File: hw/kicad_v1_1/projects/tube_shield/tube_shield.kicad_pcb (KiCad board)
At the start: 2 copper layers, 100 x 75 mm, 25 parts, among them P1 CONN_02X12_isolate_hv, P2 CONN_01X01, P3 CONN_01X01, P4 CONN_01X01, P5 CONN_01X01, Q10 MPSA42, Q11 MPSA42, U1 K155ID1, U2 K155ID1, U3 K155ID1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

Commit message: Update
Begin work on updating for rev1.1.
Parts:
- removed Q10, Q11: MPSA42, TO_SOT_Packages_SMD:SOT-23_Handsoldering
- added Q1: MMBTA42, TO_SOT_Packages_SMD:SOT-23_Handsoldering, B.Cu at (126.2, 81.5)
- added Q2: MMBTA42, TO_SOT_Packages_SMD:SOT-23_Handsoldering, B.Cu at (131.2, 81.5)
- R30, R31, R32, R33: moved to B.Cu
- moved R30 27.2 mm to (126.5, 51.2), turned to 90 degrees
- moved R31 24.2 mm to (123.5, 51.2), turned to 90 degrees
- moved R2 17.0 mm to (102.2, 51.2)
- moved R33 13.7 mm to (131.5, 88.0), turned to 270 degrees
- moved R32 12.7 mm to (126.2, 88.0), turned to 270 degrees
- moved R1 12.6 mm to (136.5, 51.2), turned to 270 degrees
- moved P2 10.0 mm to (82.0, 51.0)
- moved P3 10.0 mm to (174.0, 51.0)
- moved N1 3.00 mm to (128.0, 65.2), turned to 270 degrees
- moved N2 3.00 mm to (128.0, 71.2), turned to 270 degrees
- moved R3 1.50 mm to (157.0, 51.2)
- moved R10 0.25 mm to (97.2, 51.2)
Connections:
- P1 pad 10: /Nixie Control/N1_SEL_C -> /Nixie Control/N2_SEL_C
- P1 pad 11: /Nixie Control/N0_SEL_D -> /Nixie Control/N3_SEL_D
- P1 pad 12: /Nixie Control/N1_SEL_D -> /Nixie Control/N2_SEL_D
- P1 pad 13: /Nixie Control/N2_SEL_A -> /Nixie Control/N0_SEL_A
- P1 pad 14: /Nixie Control/N3_SEL_A -> /Nixie Control/N1_SEL_A
- P1 pad 15: /Nixie Control/N2_SEL_B -> /Nixie Control/N0_SEL_B
- P1 pad 16: /Nixie Control/N3_SEL_B -> /Nixie Control/N1_SEL_B
- P1 pad 17: /Nixie Control/N2_SEL_C -> /Nixie Control/N0_SEL_C
- P1 pad 18: /Nixie Control/N3_SEL_C -> /Nixie Control/N1_SEL_C
- P1 pad 19: /Nixie Control/N2_SEL_D -> /Nixie Control/N0_SEL_D
- P1 pad 20: /Nixie Control/N3_SEL_D -> /Nixie Control/N1_SEL_D
- P1 pad 21: /Colon Tubes/SEL_COL -> +5V
- P1 pad 22: +5V -> /Colon Tubes/SEL_COL
- P1 pad 5: /Nixie Control/N0_SEL_A -> /Nixie Control/N3_SEL_A
- P1 pad 6: /Nixie Control/N1_SEL_A -> /Nixie Control/N2_SEL_A
- P1 pad 7: /Nixie Control/N0_SEL_B -> /Nixie Control/N3_SEL_B
- P1 pad 8: /Nixie Control/N1_SEL_B -> /Nixie Control/N2_SEL_B
- P1 pad 9: /Nixie Control/N0_SEL_C -> /Nixie Control/N3_SEL_C
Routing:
- net GND: track 0.00 -> 238.0 mm, vias 0 -> 6
- net +5V: track 0.00 -> 132.4 mm, vias 0 -> 3
- net +180V: track 0.00 -> 93.3 mm, vias 0 -> 1
- net /Nixie Tubes/N3_CAT7: track 0.00 -> 55.3 mm
- net /Nixie Tubes/N0_CAT8: track 0.00 -> 55.0 mm
- net /Nixie Tubes/N1_CAT5: track 0.00 -> 54.9 mm, vias 0 -> 1
- net /Nixie Tubes/N2_CAT5: track 0.00 -> 50.2 mm, vias 0 -> 1
- net /Nixie Tubes/N0_CAT5: track 0.00 -> 49.5 mm
- net /Nixie Tubes/N3_CAT6: track 0.00 -> 49.1 mm
- net /Nixie Tubes/N0_CAT9: track 0.00 -> 48.9 mm
- net /Nixie Control/N0_SEL_B: track 0.00 -> 47.6 mm, vias 0 -> 1
- net /Nixie Tubes/N0_CAT6: track 0.00 -> 47.1 mm, vias 0 -> 1
- net /Nixie Control/N0_SEL_C: track 0.00 -> 46.0 mm, vias 0 -> 1
- net /Nixie Control/N0_SEL_A: track 0.00 -> 45.2 mm, vias 0 -> 1
- net /Nixie Tubes/N1_CAT4: track 0.00 -> 44.7 mm, vias 0 -> 1
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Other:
- board size 100 x 75 mm -> 100 x 65 mm
- net class power: clearance 0.4 -> 0.2

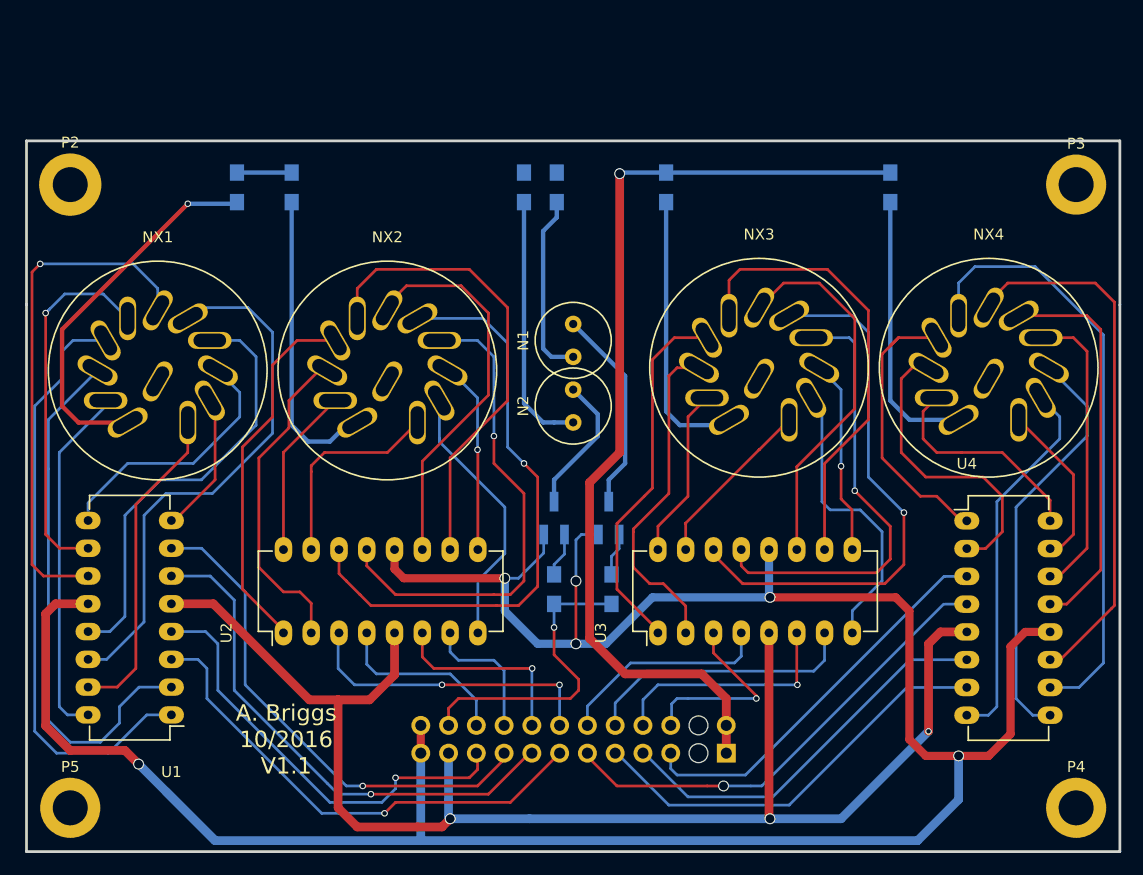
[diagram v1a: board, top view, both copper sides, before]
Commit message: Complete with errors
Check in before moving header. Currently the headers don't match up. If
I'm going to connect them with standard header I need to move it
significantly. Check in as a roll back point.
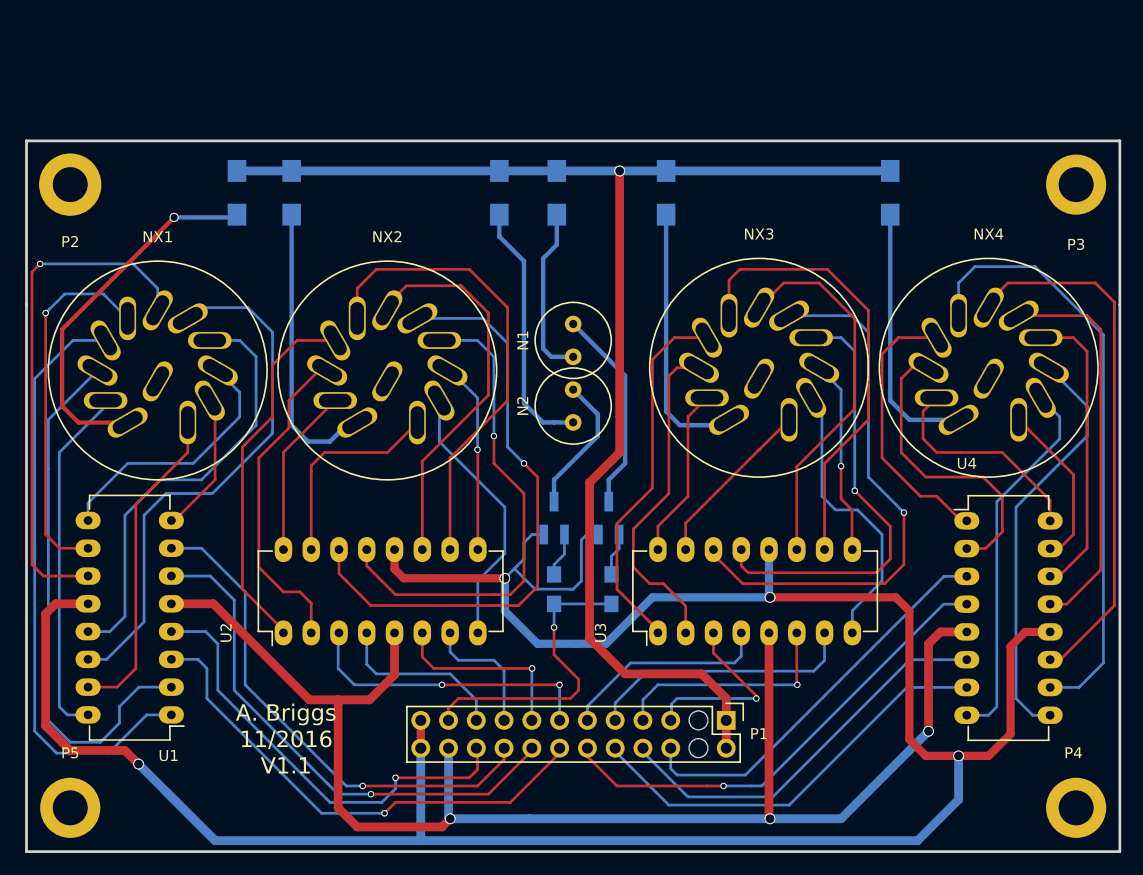
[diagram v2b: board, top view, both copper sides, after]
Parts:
- P1: moved to F.Cu
- R1, R10, R2, R3: footprint Resistors_SMD:R_0805_HandSoldering -> Resistors_SMD:R_1206_HandSoldering
- R30, R31: value 24k -> 100k; footprint Resistors_SMD:R_0805_HandSoldering -> Resistors_SMD:R_1206_HandSoldering
- moved P1 3.00 mm to (142.0, 100.0), turned to 270 degrees
- moved R31 2.30 mm to (121.2, 51.8)
- moved R1 0.50 mm to (136.5, 51.8)
- moved R10 0.50 mm to (97.2, 51.8)
- moved R2 0.50 mm to (102.2, 51.8)
- moved R3 0.50 mm to (157.0, 51.8)
- moved R30 0.50 mm to (126.5, 51.8)
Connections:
- NX1 pad 12: Net-(NX1-Pad12) -> (no net)
- NX2 pad 12: Net-(NX2-Pad12) -> (no net)
- NX3 pad 12: Net-(NX3-Pad12) -> (no net)
- NX4 pad 12: Net-(NX4-Pad12) -> (no net)
- P1 pad 10: /Nixie Control/N2_SEL_C -> /N3_SEL_C
- P1 pad 11: /Nixie Control/N3_SEL_D -> /N2_SEL_D
- P1 pad 12: /Nixie Control/N2_SEL_D -> /N3_SEL_D
- P1 pad 13: /Nixie Control/N0_SEL_A -> /N1_SEL_A
- P1 pad 14: /Nixie Control/N1_SEL_A -> /N0_SEL_A
- P1 pad 15: /Nixie Control/N0_SEL_B -> /N1_SEL_B
- P1 pad 16: /Nixie Control/N1_SEL_B -> /N0_SEL_B
- P1 pad 17: /Nixie Control/N0_SEL_C -> /N1_SEL_C
- P1 pad 18: /Nixie Control/N1_SEL_C -> /N0_SEL_C
- P1 pad 19: /Nixie Control/N0_SEL_D -> /N1_SEL_D
- P1 pad 20: /Nixie Control/N1_SEL_D -> /N0_SEL_D
- P1 pad 21: +5V -> /COL_SEL
- P1 pad 22: /Colon Tubes/SEL_COL -> +5V
- P1 pad 5: /Nixie Control/N3_SEL_A -> /N2_SEL_A
- P1 pad 6: /Nixie Control/N2_SEL_A -> /N3_SEL_A
- P1 pad 7: /Nixie Control/N3_SEL_B -> /N2_SEL_B
- P1 pad 8: /Nixie Control/N2_SEL_B -> /N3_SEL_B
- P1 pad 9: /Nixie Control/N3_SEL_C -> /N2_SEL_C
- P2 pad 1: Net-(P2-Pad1) -> (no net)
- P3 pad 1: Net-(P3-Pad1) -> (no net)
- P4 pad 1: Net-(P4-Pad1) -> (no net)
- P5 pad 1: Net-(P5-Pad1) -> (no net)
- R32 pad 2: /Colon Tubes/SEL_COL -> /COL_SEL
- R33 pad 2: /Colon Tubes/SEL_COL -> /COL_SEL
- U1 pad 3: /Nixie Control/N0_SEL_A -> /N0_SEL_A
- U1 pad 4: /Nixie Control/N0_SEL_D -> /N0_SEL_D
- U1 pad 6: /Nixie Control/N0_SEL_B -> /N0_SEL_B
- U1 pad 7: /Nixie Control/N0_SEL_C -> /N0_SEL_C
- U2 pad 3: /Nixie Control/N1_SEL_A -> /N1_SEL_A
- U2 pad 4: /Nixie Control/N1_SEL_D -> /N1_SEL_D
- U2 pad 6: /Nixie Control/N1_SEL_B -> /N1_SEL_B
- U2 pad 7: /Nixie Control/N1_SEL_C -> /N1_SEL_C
- U3 pad 3: /Nixie Control/N2_SEL_A -> /N2_SEL_A
- U3 pad 4: /Nixie Control/N2_SEL_D -> /N2_SEL_D
- U3 pad 6: /Nixie Control/N2_SEL_B -> /N2_SEL_B
- U3 pad 7: /Nixie Control/N2_SEL_C -> /N2_SEL_C
- U4 pad 3: /Nixie Control/N3_SEL_A -> /N3_SEL_A
- U4 pad 4: /Nixie Control/N3_SEL_D -> /N3_SEL_D
- U4 pad 6: /Nixie Control/N3_SEL_B -> /N3_SEL_B
- U4 pad 7: /Nixie Control/N3_SEL_C -> /N3_SEL_C
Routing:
- net /Nixie Control/N0_SEL_B: track 47.6 -> 0.00 mm, vias 1 -> 0
- net /N0_SEL_B: track 0.00 -> 47.6 mm, vias 0 -> 1
- net /Nixie Control/N0_SEL_C: track 46.0 -> 0.00 mm, vias 1 -> 0
- net /N0_SEL_C: track 0.00 -> 46.0 mm, vias 0 -> 1
- net /Nixie Control/N0_SEL_A: track 45.2 -> 0.00 mm, vias 1 -> 0
- net /N0_SEL_A: track 0.00 -> 45.2 mm, vias 0 -> 1
- net /Nixie Control/N3_SEL_D: track 42.9 -> 0.00 mm, vias 1 -> 0
- net /N3_SEL_D: track 0.00 -> 42.9 mm, vias 0 -> 1
- net /Nixie Control/N0_SEL_D: track 40.3 -> 0.00 mm, vias 1 -> 0
- net /N0_SEL_D: track 0.00 -> 40.3 mm, vias 0 -> 1
- net /Nixie Control/N3_SEL_C: track 38.6 -> 0.00 mm
- net /N3_SEL_C: track 0.00 -> 38.6 mm
- net /Nixie Control/N3_SEL_B: track 36.5 -> 0.00 mm
- net /N3_SEL_B: track 0.00 -> 36.5 mm
- net /N3_SEL_A: track 0.00 -> 36.4 mm
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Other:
- board text added: "A. Briggs 11/2016 V1.1"
- board text removed: "A. Briggs 10/2016 V1.1"

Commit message: Final Release
Update with trimming and bug fixes. This is what is being delivered as a
V1.1.0 release.
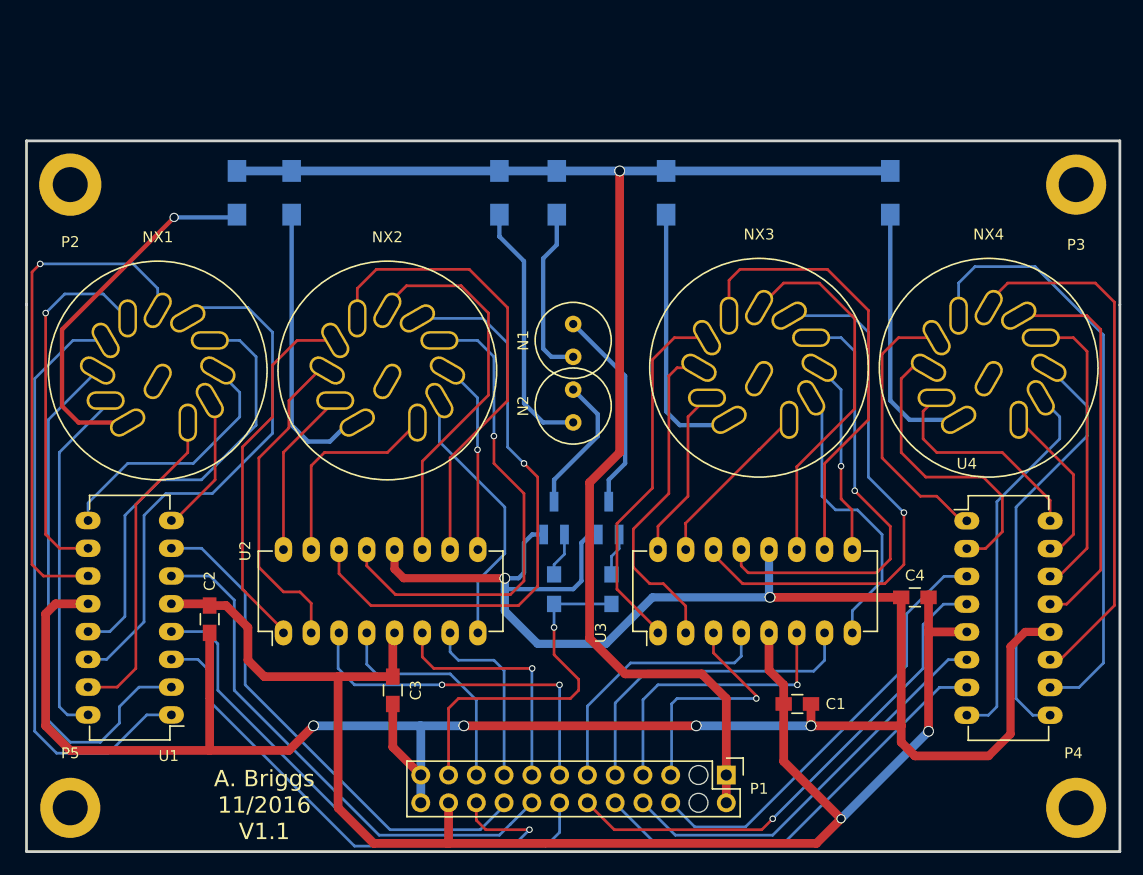
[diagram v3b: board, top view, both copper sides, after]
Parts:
- added C1: 0.1u, Capacitors_SMD:C_0805_HandSoldering, F.Cu at (148.5, 98.5)
- added C2: 0.1u, Capacitors_SMD:C_0805_HandSoldering, F.Cu at (94.8, 90.8)
- added C3: 0.1u, Capacitors_SMD:C_0805_HandSoldering, F.Cu at (111.5, 97.2)
- added C4: 0.1u, Capacitors_SMD:C_0805_HandSoldering, F.Cu at (159.2, 88.8)
- moved P1 5.00 mm to (142.0, 105.0)
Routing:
- net /N0_SEL_D: track 40.3 -> 50.4 mm
- net +5V: track 132.5 -> 140.4 mm, vias 3 -> 2
- net /N2_SEL_C: track 25.3 -> 29.9 mm
- net /N2_SEL_D: track 19.9 -> 24.4 mm
- net /N2_SEL_B: track 21.8 -> 26.3 mm
- net /N2_SEL_A: track 17.6 -> 22.1 mm
- net /N1_SEL_D: track 16.6 -> 21.1 mm
- net /N1_SEL_C: track 12.4 -> 17.0 mm
- net /N1_SEL_B: track 17.9 -> 22.4 mm
- net /COL_SEL: track 28.2 -> 32.8 mm
- net /N1_SEL_A: track 27.9 -> 32.4 mm
- net +180V: track 128.7 -> 133.0 mm
- net /N3_SEL_A: track 36.4 -> 40.4 mm
- net /N3_SEL_D: track 42.9 -> 46.6 mm
- net /N0_SEL_A: track 45.2 -> 47.4 mm, vias 1 -> 0
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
